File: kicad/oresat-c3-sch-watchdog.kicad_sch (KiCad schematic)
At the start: 35 parts, among them U28 TLV1704AIPWR

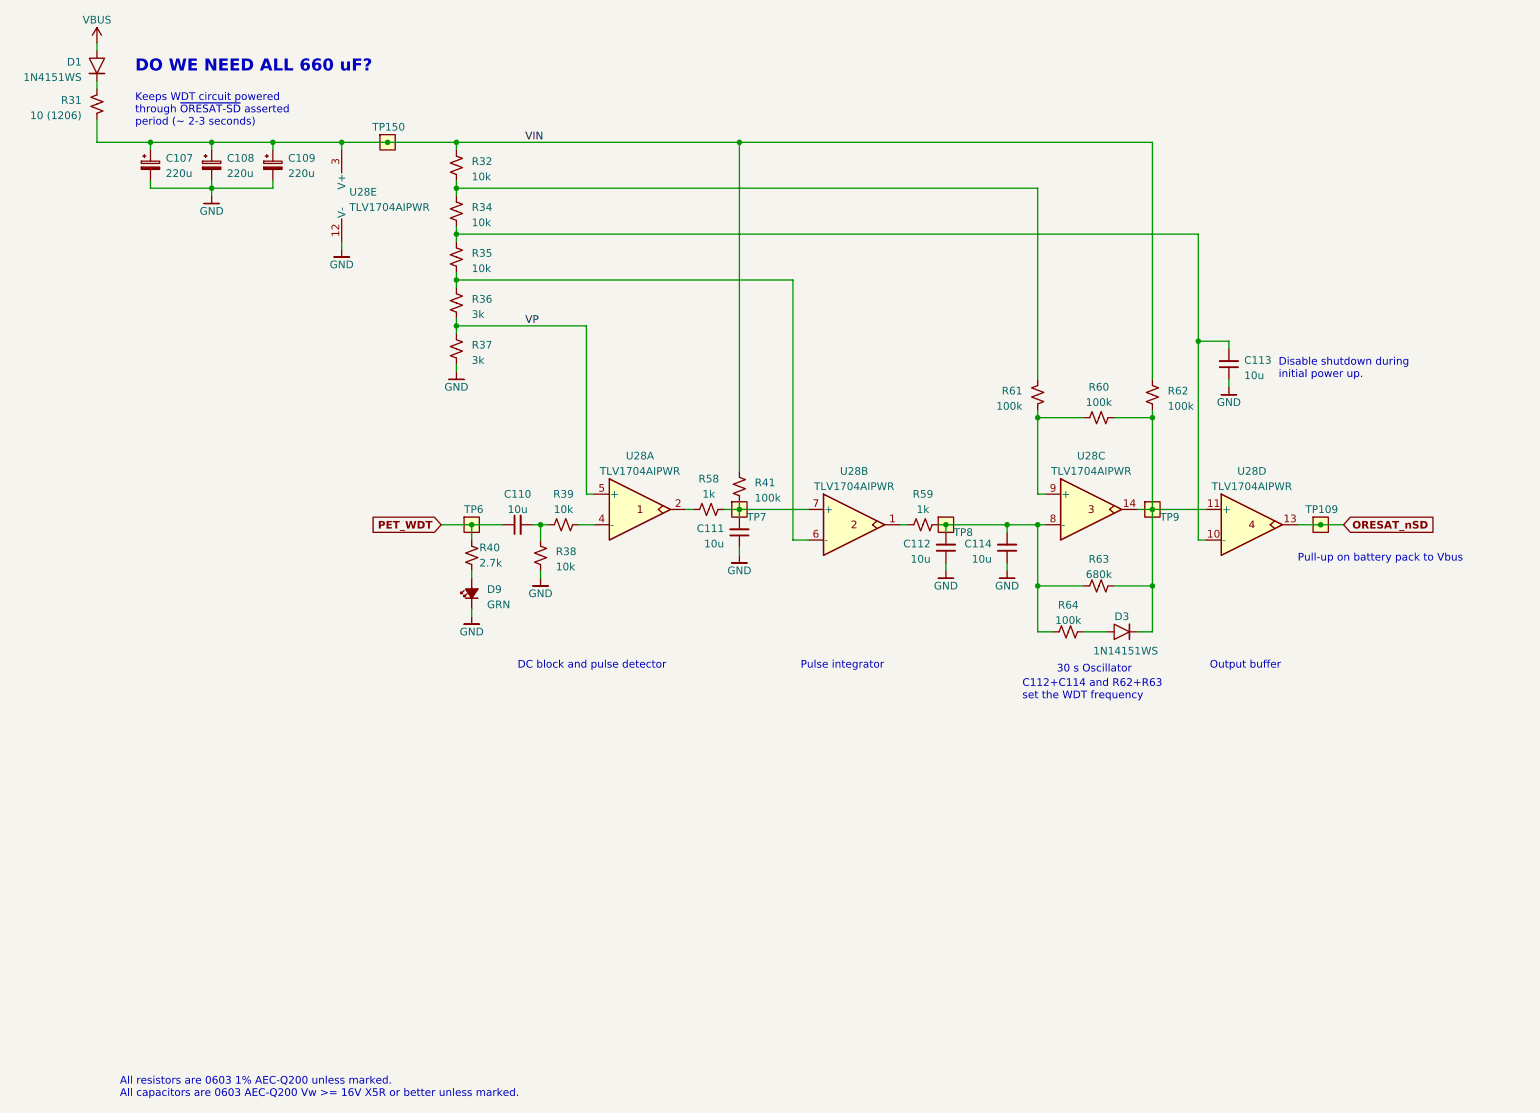
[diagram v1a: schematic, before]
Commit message: Fixed footprints and laid out WDT and OPD circuitry.
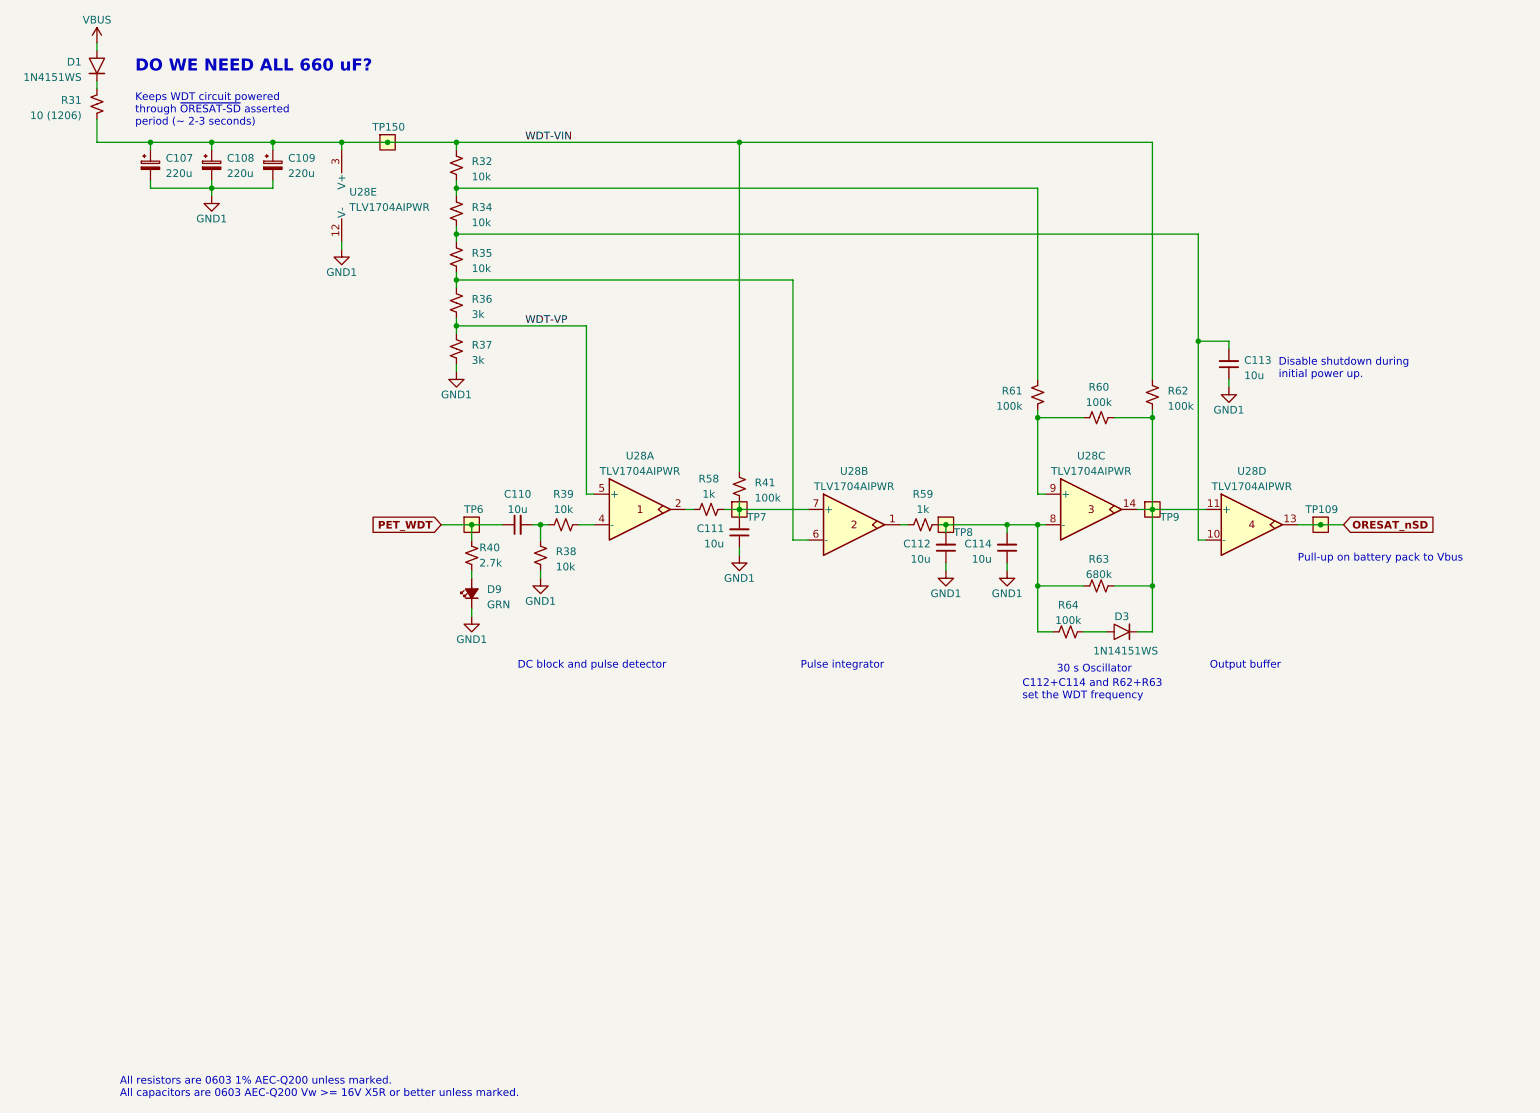
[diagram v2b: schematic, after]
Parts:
- C107, C108, C109: footprint (none) -> Capacitor_Tantalum_SMD:CP_EIA-7343-31_Kemet-D
- C110, C111, C112, C113, C114: footprint (none) -> Capacitor_SMD:C_0603_1608Metric
- D9: footprint (none) -> LED_SMD:LED_0603_1608Metric
- R31: footprint (none) -> Resistor_SMD:R_1206_3216Metric
- R32, R34, R35, R36, R37, R38, R39, R40, R41, R58, R59, R60, R61, R62, R63, R64: footprint (none) -> Resistor_SMD:R_0603_1608Metric
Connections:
- net VBUS: now also D1.2; no longer D1. (2)
- net at R64.1: now also D3.2; no longer D3. (2)
- net at R60.2, R62.1, R63.1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: now also D3.1; no longer D3. (2)
- net at R31.1: now also D1.1; no longer D1. (2)
- net GND renamed GND1
- net VIN renamed WDT-VIN
- net VP renamed WDT-VP

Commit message: Switched all grounds to a single ground, because I can't find a way to overlap ground planes in KiCAD. That's actually not terrible, however, because KiCAD has an anti-plane feature which I used to cut the ground plane between UHF and L radios and L radio and Octavo. So actually I think it came out better than having separate ground planes. Only thing left now are the ~ 40 connections to the Octavo.
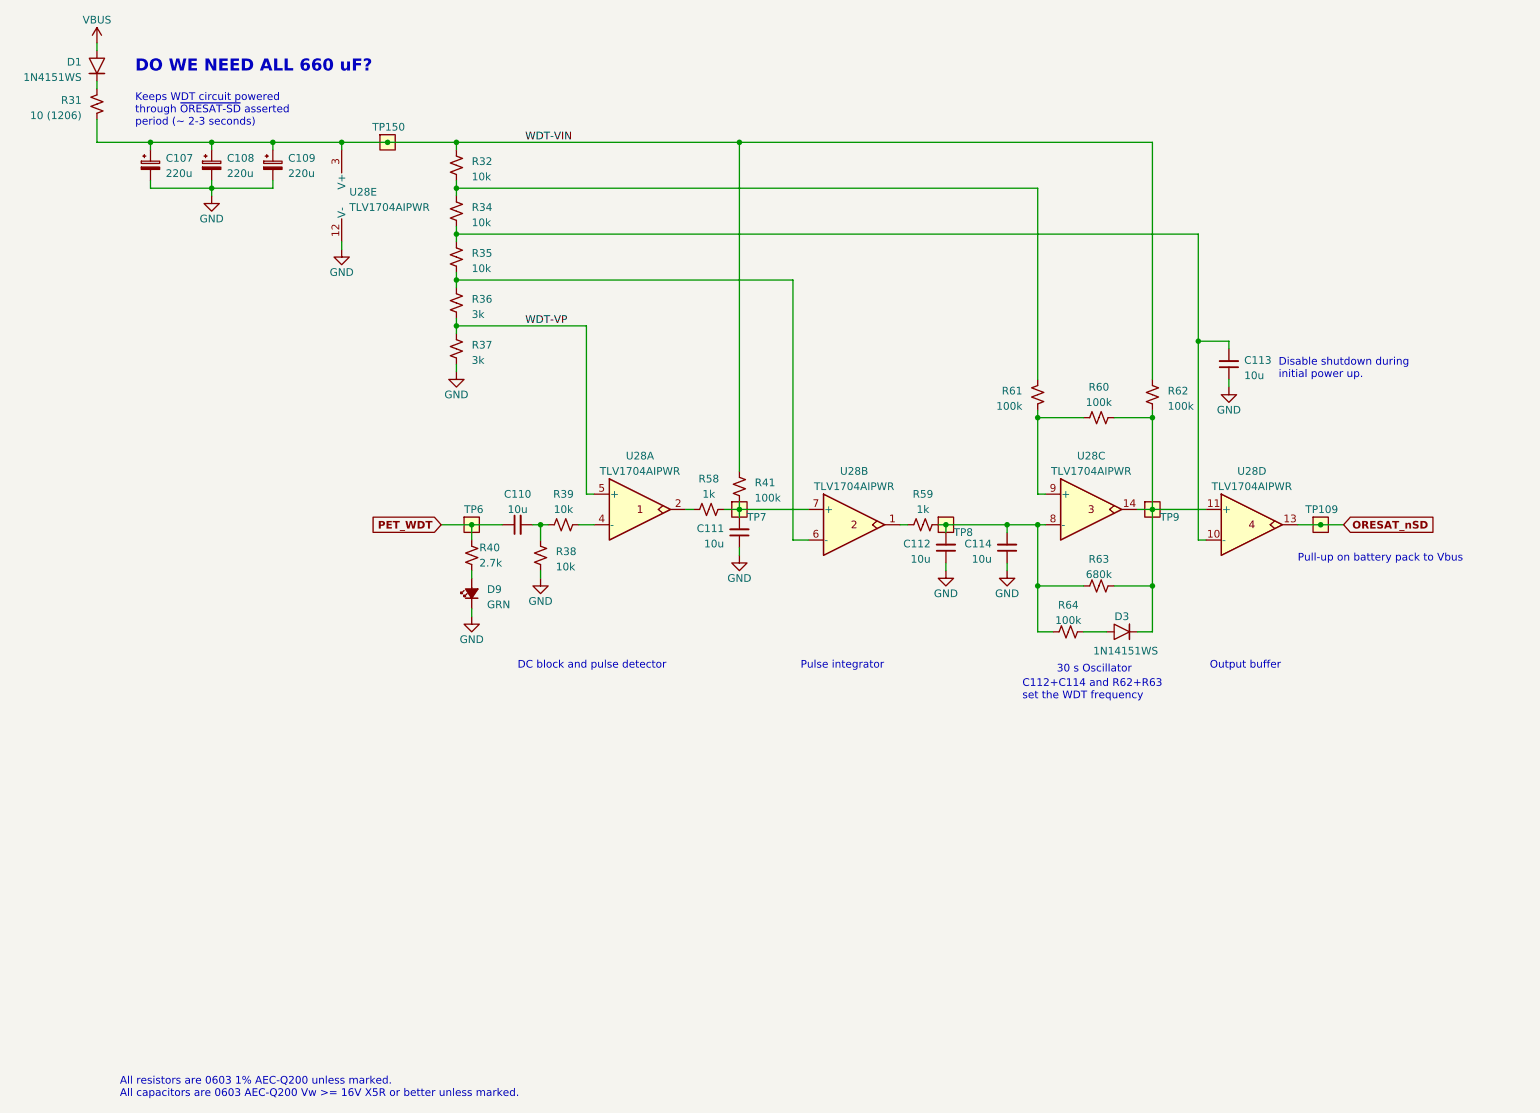
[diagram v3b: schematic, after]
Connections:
- net GND1 renamed GND
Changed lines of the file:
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@@
     )
   )
-  (symbol (lib_id "power:GND1") (at 177.8 180.34 0) (unit 1)
+  (symbol (lib_id "power:GND") (at 177.8 180.34 0) (unit 1)
     (in_bom yes) (on_board yes) (dnp no)
     (property "Reference" "#GND0163" (at 177.8 186.69 0)
       (effects (font (size 1.27 1.27)) hide)
     )
-    (property "Value" "GND1" (at 177.8 184.15 0)
+    (property "Value" "GND" (at 177.8 184.15 0)
       (effects (font (size 1.27 1.27)))
     )
@@
         )
         (path "/65d12cdd-c326-4033-9053-c59fa4e0b25e/730a6f7e-0bbd-44c5-a45a-78e61e54b6d6"
-          (reference "#PWR0163") (unit 1)
+          (reference "#PWR?") (unit 1)
         )
       )
@@
     )
   )
-  (symbol (lib_id "power:GND1") (at 134.62 110.49 0) (unit 1)
+  (symbol (lib_id "power:GND") (at 134.62 110.49 0) (unit 1)
     (in_bom yes) (on_board yes) (dnp no)
     (property "Reference" "#GND0163" (at 134.62 116.84 0)
       (effects (font (size 1.27 1.27)) hide)
     )
-    (property "Value" "GND1" (at 134.62 114.3 0)
+    (property "Value" "GND" (at 134.62 114.3 0)
       (effects (font (size 1.27 1.27)))
     )
@@
         )
         (path "/65d12cdd-c326-4033-9053-c59fa4e0b25e/730a6f7e-0bbd-44c5-a45a-78e61e54b6d6"
-          (reference "#PWR0169") (unit 1)
+          (reference "#PWR?") (unit 1)
         )
       )
@@
     )
   )
-  (symbol (lib_id "power:GND1") (at 189.23 173.99 0) (unit 1)
+  (symbol (lib_id "power:GND") (at 189.23 173.99 0) (unit 1)
     (in_bom yes) (on_board yes) (dnp no)
     (property "Reference" "#GND0163" (at 189.23 180.34 0)
       (effects (font (size 1.27 1.27)) hide)
     )
-    (property "Value" "GND1" (at 189.23 177.8 0)
+    (property "Value" "GND" (at 189.23 177.8 0)
       (effects (font (size 1.27 1.27)))
     )
@@
         )
         (path "/65d12cdd-c326-4033-9053-c59fa4e0b25e/730a6f7e-0bbd-44c5-a45a-78e61e54b6d6"
-          (reference "#PWR0162") (unit 1)
-        )
-      )
-    )
-  )
-  (symbol (lib_id "power:GND1") (at 156.21 119.38 0) (mirror y) (unit 1)
+          (reference "#PWR?") (unit 1)
+        )
+      )
+    )
+  )
+  (symbol (lib_id "power:GND") (at 156.21 119.38 0) (mirror y) (unit 1)
     (in_bom yes) (on_board yes) (dnp no)
     (property "Reference" "#GND0163" (at 156.21 125.73 0)
       (effects (font (size 1.27 1.27)) hide)
     )
-    (property "Value" "GND1" (at 156.21 123.19 0)
+    (property "Value" "GND" (at 156.21 123.19 0)
       (effects (font (size 1.27 1.27)))
     )
@@
         )
         (path "/65d12cdd-c326-4033-9053-c59fa4e0b25e/730a6f7e-0bbd-44c5-a45a-78e61e54b6d6"
-          (reference "#PWR0167") (unit 1)
+          (reference "#PWR?") (unit 1)
         )
       )
@@
     )
   )
-  (symbol (lib_id "power:GND1") (at 175.26 139.7 0) (unit 1)
+  (symbol (lib_id "power:GND") (at 175.26 139.7 0) (unit 1)
     (in_bom yes) (on_board yes) (dnp no)
     (property "Reference" "#GND0163" (at 175.26 146.05 0)
       (effects (font (size 1.27 1.27)) hide)
     )
-    (property "Value" "GND1" (at 175.26 143.51 0)
+    (property "Value" "GND" (at 175.26 143.51 0)
       (effects (font (size 1.27 1.27)))
     )
@@
         )
         (path "/65d12cdd-c326-4033-9053-c59fa4e0b25e/730a6f7e-0bbd-44c5-a45a-78e61e54b6d6"
-          (reference "#PWR0168") (unit 1)
+          (reference "#PWR?") (unit 1)
         )
       )
@@
     )
   )
-  (symbol (lib_id "power:GND1") (at 256.54 172.72 0) (mirror y) (unit 1)
+  (symbol (lib_id "power:GND") (at 256.54 172.72 0) (mirror y) (unit 1)
     (in_bom yes) (on_board yes) (dnp no)
     (property "Reference" "#GND0163" (at 256.54 179.07 0)
       (effects (font (size 1.27 1.27)) hide)
     )
-    (property "Value" "GND1" (at 256.54 176.53 0)
+    (property "Value" "GND" (at 256.54 176.53 0)
       (effects (font (size 1.27 1.27)))
     )
@@
         )
         (path "/65d12cdd-c326-4033-9053-c59fa4e0b25e/730a6f7e-0bbd-44c5-a45a-78e61e54b6d6"
-          (reference "#PWR0164") (unit 1)
+          (reference "#PWR?") (unit 1)
         )
       )
@@
     )
   )
-  (symbol (lib_id "power:GND1") (at 303.53 142.24 0) (mirror y) (unit 1)
+  (symbol (lib_id "power:GND") (at 303.53 142.24 0) (mirror y) (unit 1)
     (in_bom yes) (on_board yes) (dnp no)
     (property "Reference" "#GND0163" (at 303.53 148.59 0)
       (effects (font (size 1.27 1.27)) hide)
     )
-    (property "Value" "GND1" (at 303.53 146.05 0)
+    (property "Value" "GND" (at 303.53 146.05 0)
       (effects (font (size 1.27 1.27)))
     )
@@
         )
         (path "/65d12cdd-c326-4033-9053-c59fa4e0b25e/730a6f7e-0bbd-44c5-a45a-78e61e54b6d6"
-          (reference "#PWR0170") (unit 1)
+          (reference "#PWR?") (unit 1)
         )
       )
@@
     )
   )
-  (symbol (lib_id "power:GND1") (at 266.7 172.72 0) (mirror y) (unit 1)
+  (symbol (lib_id "power:GND") (at 266.7 172.72 0) (mirror y) (unit 1)
     (in_bom yes) (on_board yes) (dnp no)
     (property "Reference" "#GND0163" (at 266.7 179.07 0)
       (effects (font (size 1.27 1.27)) hide)
     )
-    (property "Value" "GND1" (at 266.7 176.53 0)
+    (property "Value" "GND" (at 266.7 176.53 0)
       (effects (font (size 1.27 1.27)))
     )
@@
         )
         (path "/65d12cdd-c326-4033-9053-c59fa4e0b25e/730a6f7e-0bbd-44c5-a45a-78e61e54b6d6"
-          (reference "#PWR0165") (unit 1)
+          (reference "#PWR?") (unit 1)
         )
       )
@@
     )
   )
-  (symbol (lib_id "power:GND1") (at 222.25 170.18 0) (unit 1)
+  (symbol (lib_id "power:GND") (at 222.25 170.18 0) (unit 1)
     (in_bom yes) (on_board yes) (dnp no)
     (property "Reference" "#GND0163" (at 222.25 176.53 0)
       (effects (font (size 1.27 1.27)) hide)
     )
-    (property "Value" "GND1" (at 222.25 173.99 0)
+    (property "Value" "GND" (at 222.25 173.99 0)
       (effects (font (size 1.27 1.27)))
     )
@@
         )
         (path "/65d12cdd-c326-4033-9053-c59fa4e0b25e/730a6f7e-0bbd-44c5-a45a-78e61e54b6d6"
-          (reference "#PWR0166") (unit 1)
-        )
-      )
+          (reference "#PWR?") (unit 1)
+        )
+      )
